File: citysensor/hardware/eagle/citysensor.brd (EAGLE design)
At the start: 65.7 x 31.7 mm, 33 parts, among them U1 ATMEGA328P_TQFP, X1 16MHZ

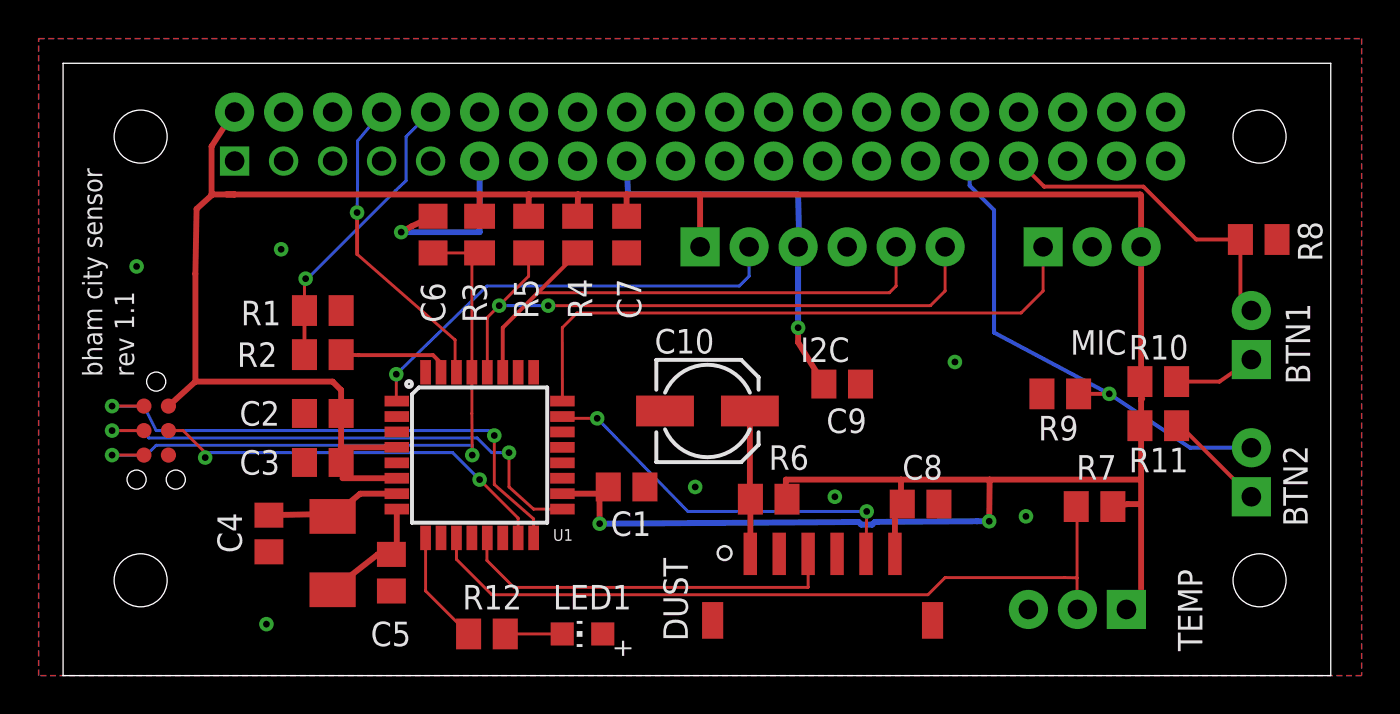
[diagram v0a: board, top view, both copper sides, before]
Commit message: Moved Button connectors away from screw keepout, fixed backwards LED1, rearranged SMD resistors around button connectors. No reported DRC/ERC errors
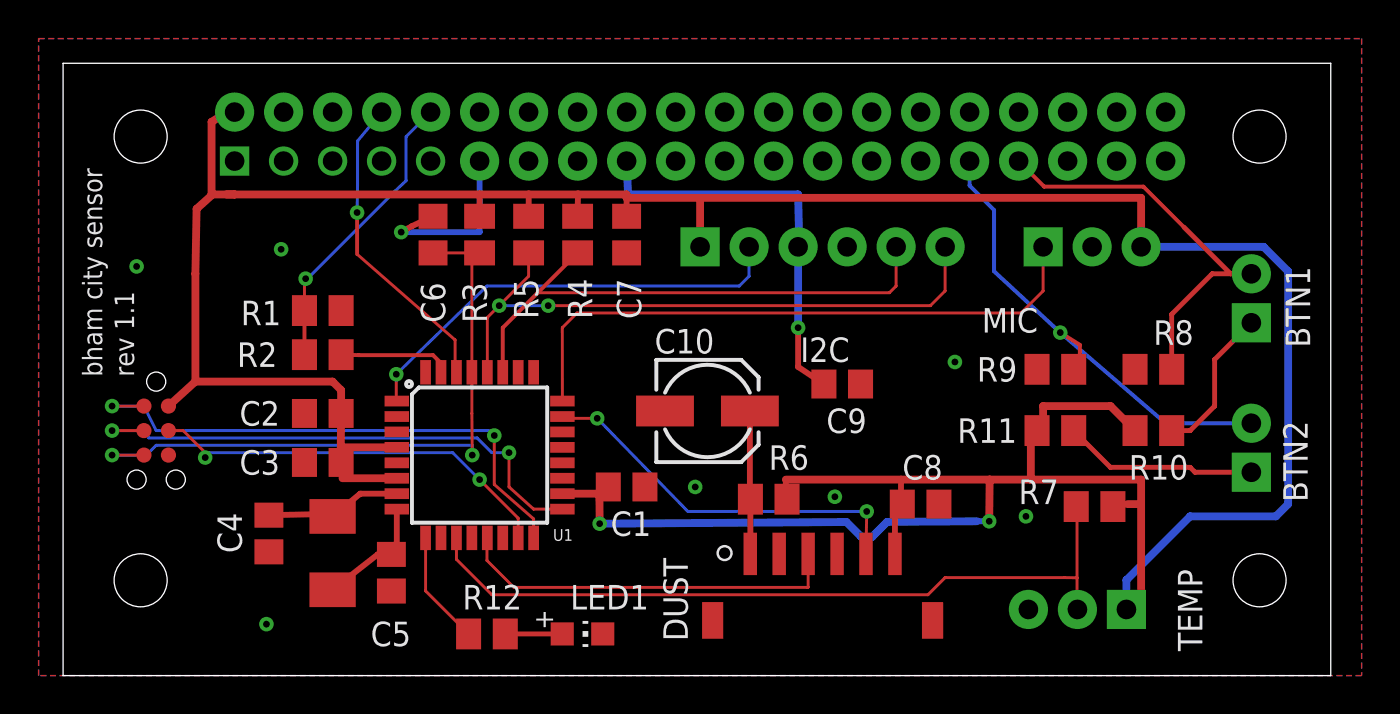
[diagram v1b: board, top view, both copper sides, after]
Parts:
- moved R8 8.67 mm to (56.5, 14.6), turned to 180 degrees
- moved R11 5.34 mm to (51.4, 11.4)
- moved R10 2.55 mm to (56.5, 11.4)
- moved BTN1 1.91 mm to (61.6, 18.3)
- moved R9 1.30 mm to (51.4, 14.6)
- moved BTN2 1.27 mm to (61.6, 10.5)
- turned LED1 to 270 degrees
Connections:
- net GND: now also LED1.C; no longer LED1.A
- net N$4: now also LED1.A; no longer LED1.C
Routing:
- net VCC: track 166.2 -> 195.8 mm
- net N$2: track 5.40 -> 10.1 mm
- net BTN1OUT: track 17.1 -> 21.3 mm
- net N$1: track 4.23 -> 7.86 mm
- net BTN2OUT: track 26.0 -> 25.4 mm
